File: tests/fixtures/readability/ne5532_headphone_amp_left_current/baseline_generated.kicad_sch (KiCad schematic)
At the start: 13 parts, among them J1 AudioIn_L, J2 AudioIn_R, J3 PowerSupply, J4 HeadphoneOut_L, J5 HeadphoneOut_R

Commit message: Fix NE5532 real-fixture multi-unit regressions
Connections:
- net at R6.2 (B): now also R2.2 (B), R8.1 (A)
- net at R1.2 (B), R5.1 (A): no longer R5.2 (B), R7.1 (A)
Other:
- note added: "OpenClaw:generated=v1"
- note added: "OpenClaw:region=managed"

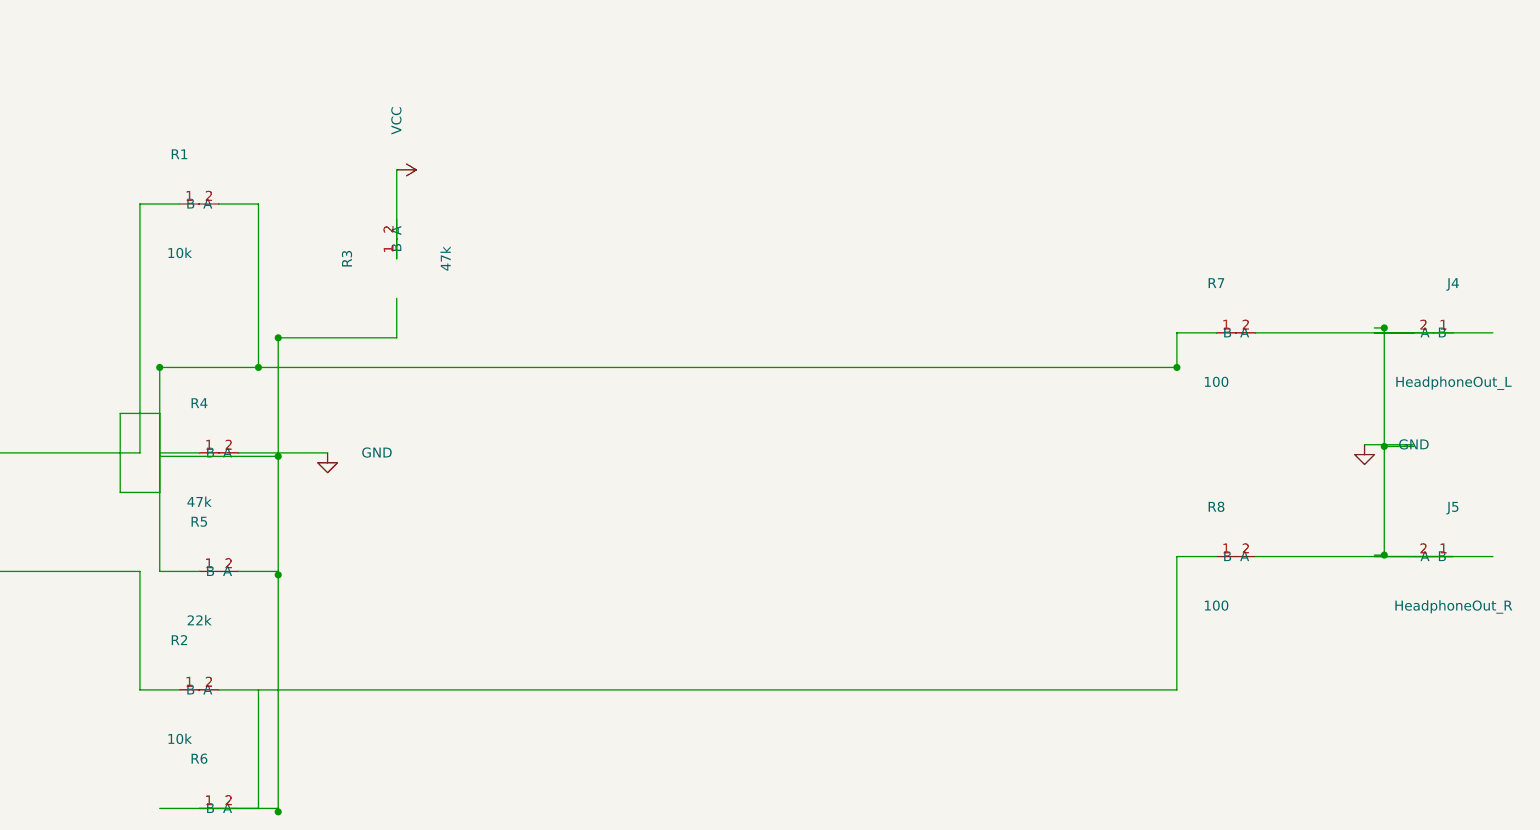
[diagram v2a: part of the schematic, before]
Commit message: Refine block role taxonomy and layout grouping
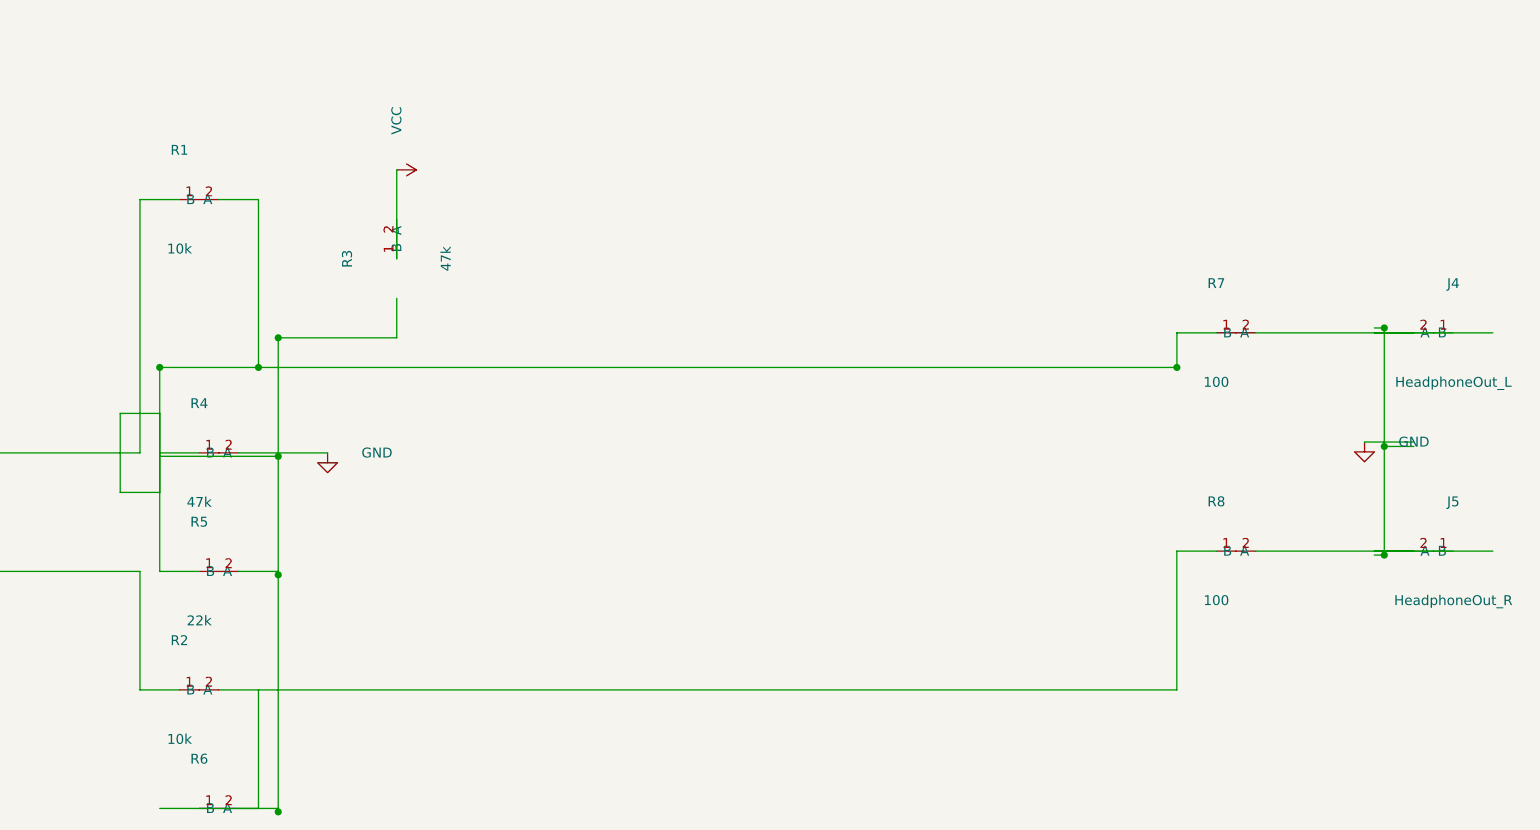
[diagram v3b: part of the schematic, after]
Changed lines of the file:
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@@
         "BaselineHeadphoneAmp"
         (path
-          "/5d1cf440-5ad4-4c6d-8be3-92aafc95d77a/"
+          "/ac586361-9cce-465f-806b-2c5b9a6e289c/"
           (reference "J1")
           (unit 1)
@@
         "BaselineHeadphoneAmp"
         (path
-          "/5d1cf440-5ad4-4c6d-8be3-92aafc95d77a/"
+          "/ac586361-9cce-465f-806b-2c5b9a6e289c/"
           (reference "J2")
           (unit 1)
@@
         "BaselineHeadphoneAmp"
         (path
-          "/5d1cf440-5ad4-4c6d-8be3-92aafc95d77a/"
+          "/ac586361-9cce-465f-806b-2c5b9a6e289c/"
           (reference "J3")
           (unit 1)
@@
         "BaselineHeadphoneAmp"
         (path
-          "/5d1cf440-5ad4-4c6d-8be3-92aafc95d77a/"
+          "/ac586361-9cce-465f-806b-2c5b9a6e289c/"
           (reference "J4")
           (unit 1)
@@
   (symbol
     (lib_id "TestLib:R")
-    (at 260.34 131.00 180)
+    (at 260.34 130.30 180)
     (unit 1)
     (exclude_from_sim yes)
@@
       "Reference"
       "J5"
-      (at 260.34 124.65 0)
+      (at 260.34 123.95 0)
       (effects (font (size 1.27 1.27)))
     )
@@
       "Value"
       "HeadphoneOut_R"
-      (at 260.34 137.35 0)
-      (effects (font (size 1.27 1.27)))
-    )
-    (property
-      "Footprint"
-      ""
-      (at 260.34 131.00 0)
-      (effects (font (size 1.27 1.27)) hide)
-    )
-    (property
-      "Datasheet"
-      "~"
-      (at 260.34 131.00 0)
+      (at 260.34 136.65 0)
+      (effects (font (size 1.27 1.27)))
+    )
+    (property
+      "Footprint"
+      ""
+      (at 260.34 130.30 0)
+      (effects (font (size 1.27 1.27)) hide)
+    )
+    (property
+      "Datasheet"
+      "~"
+      (at 260.34 130.30 0)
       (effects (font (size 1.27 1.27)) hide)
     )
@@
         "BaselineHeadphoneAmp"
         (path
-          "/5d1cf440-5ad4-4c6d-8be3-92aafc95d77a/"
+          "/ac586361-9cce-465f-806b-2c5b9a6e289c/"
           (reference "J5")
           (unit 1)
@@
   (symbol
     (lib_id "TestLib:R")
-    (at 96.52 85.66 0)
+    (at 96.52 85.09 0)
     (unit 1)
     (exclude_from_sim yes)
@@
       "Reference"
       "R1"
-      (at 96.52 79.31 0)
+      (at 96.52 78.74 0)
       (effects (font (size 1.27 1.27)))
     )
@@
       "Value"
       "10k"
-      (at 96.52 92.01 0)
-      (effects (font (size 1.27 1.27)))
-    )
-    (property
-      "Footprint"
-      ""
-      (at 96.52 85.66 0)
-      (effects (font (size 1.27 1.27)) hide)
-    )
-    (property
-      "Datasheet"
-      "~"
-      (at 96.52 85.66 0)
+      (at 96.52 91.44 0)
+      (effects (font (size 1.27 1.27)))
+    )
+    (property
+      "Footprint"
+      ""
+      (at 96.52 85.09 0)
+      (effects (font (size 1.27 1.27)) hide)
+    )
+    (property
+      "Datasheet"
+      "~"
+      (at 96.52 85.09 0)
       (effects (font (size 1.27 1.27)) hide)
     )
@@
         "BaselineHeadphoneAmp"
         (path
-          "/5d1cf440-5ad4-4c6d-8be3-92aafc95d77a/"
+          "/ac586361-9cce-465f-806b-2c5b9a6e289c/"
           (reference "R1")
           (unit 1)
@@
         "BaselineHeadphoneAmp"
         (path
-          "/5d1cf440-5ad4-4c6d-8be3-92aafc95d77a/"
+          "/ac586361-9cce-465f-806b-2c5b9a6e289c/"
           (reference "R2")
           (unit 1)
@@
         "BaselineHeadphoneAmp"
         (path
-          "/5d1cf440-5ad4-4c6d-8be3-92aafc95d77a/"
+          "/ac586361-9cce-465f-806b-2c5b9a6e289c/"
           (reference "R3")
           (unit 1)
@@
         "BaselineHeadphoneAmp"
         (path
-          "/5d1cf440-5ad4-4c6d-8be3-92aafc95d77a/"
+          "/ac586361-9cce-465f-806b-2c5b9a6e289c/"
           (reference "R4")
           (unit 1)
@@
         "BaselineHeadphoneAmp"
         (path
-          "/5d1cf440-5ad4-4c6d-8be3-92aafc95d77a/"
+          "/ac586361-9cce-465f-806b-2c5b9a6e289c/"
           (reference "R5")
           (unit 1)
@@
         "BaselineHeadphoneAmp"
         (path
-          "/5d1cf440-5ad4-4c6d-8be3-92aafc95d77a/"
+          "/ac586361-9cce-465f-806b-2c5b9a6e289c/"
           (reference "R6")
           (unit 1)
@@
         "BaselineHeadphoneAmp"
         (path
-          "/5d1cf440-5ad4-4c6d-8be3-92aafc95d77a/"
+          "/ac586361-9cce-465f-806b-2c5b9a6e289c/"
           (reference "R7")
           (unit 1)
@@
   (symbol
     (lib_id "TestLib:R")
-    (at 229.86 131.00 0)
+    (at 229.86 130.30 0)
     (unit 1)
     (exclude_from_sim yes)
@@
       "Reference"
       "R8"
-      (at 229.86 124.65 0)
+      (at 229.86 123.95 0)
       (effects (font (size 1.27 1.27)))
     )
@@
       "Value"
       "100"
-      (at 229.86 137.35 0)
-      (effects (font (size 1.27 1.27)))
-    )
-    (property
-      "Footprint"
-      ""
-      (at 229.86 131.00 0)
-      (effects (font (size 1.27 1.27)) hide)
-    )
-    (property
-      "Datasheet"
-      "~"
-      (at 229.86 131.00 0)
+      (at 229.86 136.65 0)
+      (effects (font (size 1.27 1.27)))
+    )
+    (property
+      "Footprint"
+      ""
+      (at 229.86 130.30 0)
+      (effects (font (size 1.27 1.27)) hide)
+    )
+    (property
+      "Datasheet"
+      "~"
+      (at 229.86 130.30 0)
       (effects (font (size 1.27 1.27)) hide)
     )
@@
         "BaselineHeadphoneAmp"
         (path
-          "/5d1cf440-5ad4-4c6d-8be3-92aafc95d77a/"
+          "/ac586361-9cce-465f-806b-2c5b9a6e289c/"
           (reference "R8")
           (unit 1)
@@
   )
   (wire
-    (pts (xy 255.26 131.00) (xy 250.18 131.00))
+    (pts (xy 255.26 130.30) (xy 250.18 130.30))
     (stroke (width 0) (type default))
   )
@@
   )
   (wire
-    (pts (xy 255.26 116.62) (xy 248.92 116.62))
+    (pts (xy 255.26 116.27) (xy 248.92 116.27))
     (stroke (width 0) (type default))
   )
@@
   )
   (wire
-    (pts (xy 96.52 85.66) (xy 91.44 85.66))
-    (stroke (width 0) (type default))
-  )
-  (wire
-    (pts (xy 91.44 117.67) (xy 91.44 85.66))
+    (pts (xy 96.52 85.09) (xy 91.44 85.09))
+    (stroke (width 0) (type default))
+  )
+  (wire
+    (pts (xy 91.44 117.67) (xy 91.44 85.09))
     (stroke (width 0) (type default))
   )
@@
   )
   (wire
-    (pts (xy 234.94 131.00) (xy 265.42 131.00))
-    (stroke (width 0) (type default))
-  )
-  (wire
-    (pts (xy 101.60 85.66) (xy 106.68 85.66))
+    (pts (xy 234.94 130.30) (xy 265.42 130.30))
+    (stroke (width 0) (type default))
+  )
+  (wire
+    (pts (xy 101.60 85.09) (xy 106.68 85.09))
     (stroke (width 0) (type default))
   )
@@
   )
   (wire
-    (pts (xy 106.68 85.66) (xy 106.68 106.68))
+    (pts (xy 106.68 85.09) (xy 106.68 106.68))
     (stroke (width 0) (type default))
   )
@@
   )
   (wire
-    (pts (xy 229.86 131.00) (xy 224.78 131.00))
+    (pts (xy 229.86 130.30) (xy 224.78 130.30))
     (stroke (width 0) (type default))
   )
@@
   )
   (wire
-    (pts (xy 224.78 148.15) (xy 224.78 131.00))
+    (pts (xy 224.78 148.15) (xy 224.78 130.30))
     (stroke (width 0) (type default))
   )
@@
         "BaselineHeadphoneAmp"
         (path
-          "/5d1cf440-5ad4-4c6d-8be3-92aafc95d77a/"
+          "/ac586361-9cce-465f-806b-2c5b9a6e289c/"
           (reference "#PWR01")
           (unit 1)
@@
         "BaselineHeadphoneAmp"
         (path
-          "/5d1cf440-5ad4-4c6d-8be3-92aafc95d77a/"
+          "/ac586361-9cce-465f-806b-2c5b9a6e289c/"
           (reference "#PWR02")
           (unit 1)
@@
   (symbol
     (lib_id "power:GND")
-    (at 248.92 116.62 0)
+    (at 248.92 116.27 0)
     (unit 1)
     (exclude_from_sim yes)
@@
       "Reference"
       "#PWR03"
-      (at 248.92 116.62 0)
+      (at 248.92 116.27 0)
       (effects (font (size 1.27 1.27)) hide)
     )
@@
       "Value"
       "GND"
-      (at 255.27 116.62 0)
-      (effects (font (size 1.27 1.27)))
-    )
-    (property
-      "Footprint"
-      ""
-      (at 248.92 116.62 0)
-      (effects (font (size 1.27 1.27)) hide)
-    )
-    (property
-      "Datasheet"
-      "~"
-      (at 248.92 116.62 0)
-      (effects (font (size 1.27 1.27)) hide)
-    )
-    (pin "1")
-    (instances
-      (project
-        "BaselineHeadphoneAmp"
-        (path
-          "/5d1cf440-5ad4-4c6d-8be3-92aafc95d77a/"
+      (at 255.27 116.27 0)
+      (effects (font (size 1.27 1.27)))
+    )
+    (property
+      "Footprint"
+      ""
+      (at 248.92 116.27 0)
+      (effects (font (size 1.27 1.27)) hide)
+    )
+    (property
+      "Datasheet"
+      "~"
+      (at 248.92 116.27 0)
+      (effects (font (size 1.27 1.27)) hide)
+    )
+    (pin "1")
+    (instances
+      (project
+        "BaselineHeadphoneAmp"
+        (path
+          "/ac586361-9cce-465f-806b-2c5b9a6e289c/"
           (reference "#PWR03")
           (unit 1)
@@
         "BaselineHeadphoneAmp"
         (path
-          "/5d1cf440-5ad4-4c6d-8be3-92aafc95d77a/"
+          "/ac586361-9cce-465f-806b-2c5b9a6e289c/"
           (reference "#PWR04")
           (unit 1)
@@
         "BaselineHeadphoneAmp"
         (path
-          "/5d1cf440-5ad4-4c6d-8be3-92aafc95d77a/"
+          "/ac586361-9cce-465f-806b-2c5b9a6e289c/"
           (reference "#PWR05")
           (unit 1)
@@
         "BaselineHeadphoneAmp"
         (path
-          "/5d1cf440-5ad4-4c6d-8be3-92aafc95d77a/"
+          "/ac586361-9cce-465f-806b-2c5b9a6e289c/"
           (reference "#PWR06")
           (unit 1)
@@
     (effects (font (size 1.27 1.27)) (justify left) hide)
   )
-  (sheet_instances (path "/5d1cf440-5ad4-4c6d-8be3-92aafc95d77a/" (page "1")))
+  (sheet_instances (path "/ac586361-9cce-465f-806b-2c5b9a6e289c/" (page "1")))
 )

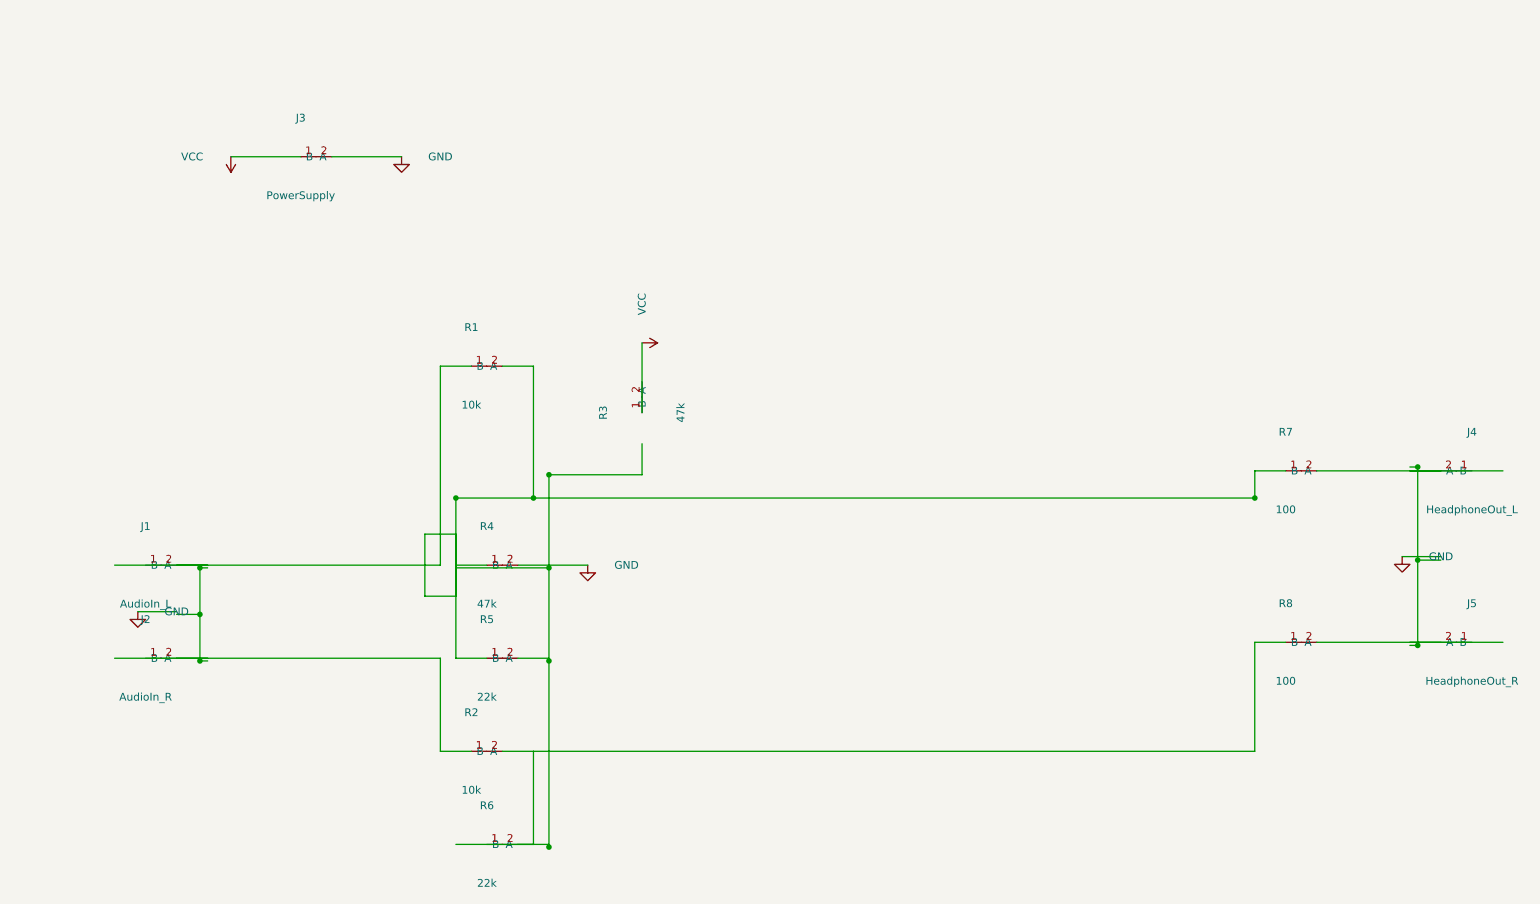
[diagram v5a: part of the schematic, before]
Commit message: feat: improve routing labels and layout snapping
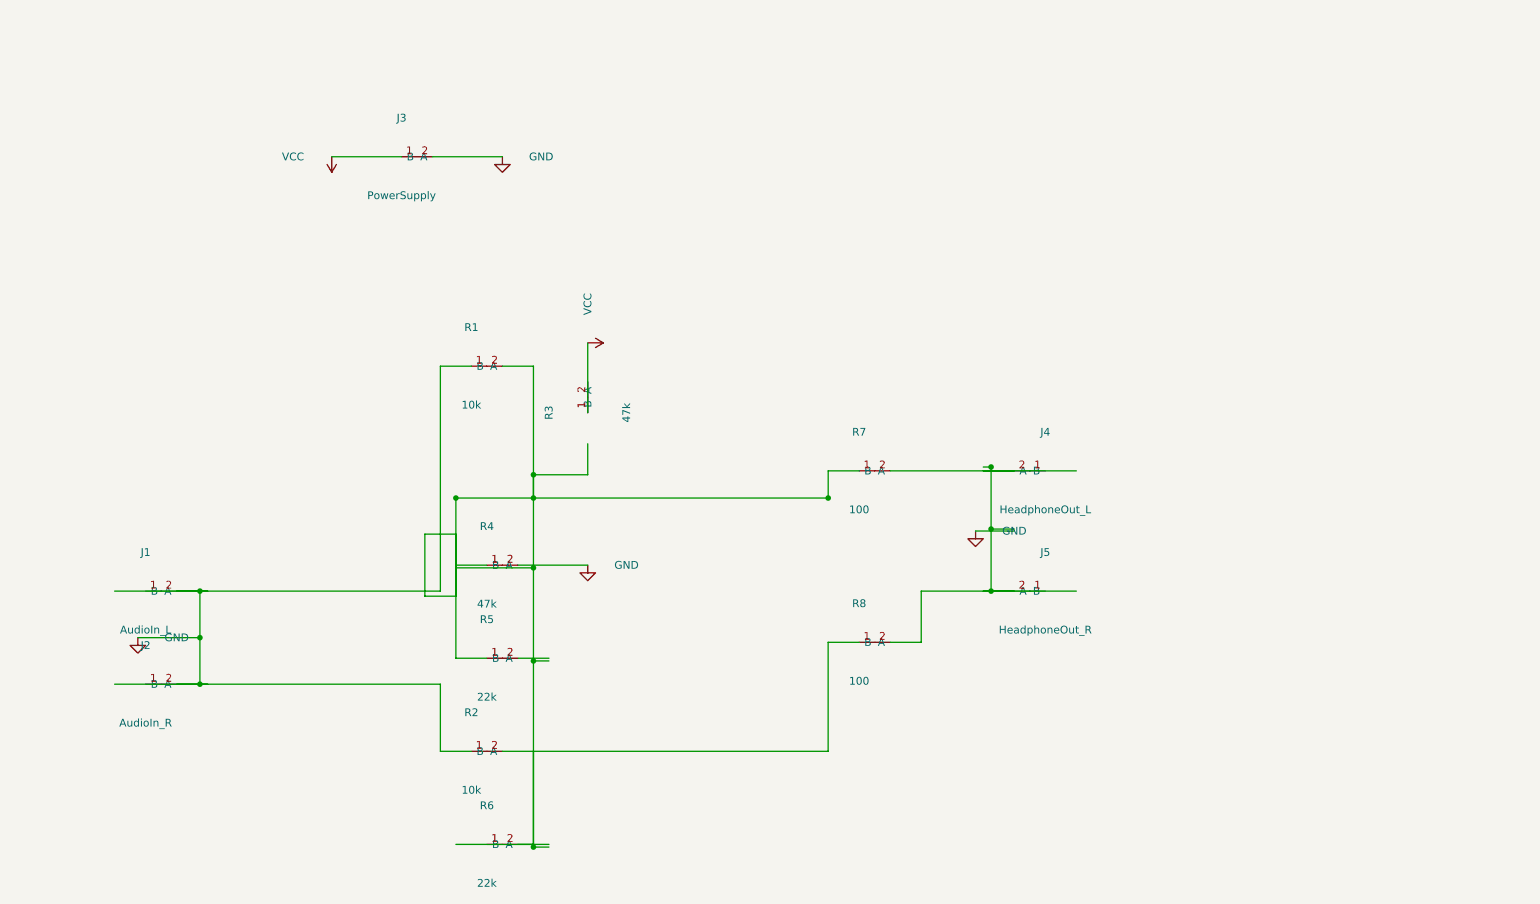
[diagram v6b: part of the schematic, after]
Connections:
- net GND: now also J1.2 (B), J2.2 (B), R1.1 (A), R2.1 (A)
- net at R1.2 (B), R5.1 (A): now also R2.2 (B), R6.2 (B), R8.1 (A)
